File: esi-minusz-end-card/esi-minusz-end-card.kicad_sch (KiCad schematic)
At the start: 26 parts, among them J1 J-SAMTEC-TFM-120-01-L-D-RA, J2 U.FL-R-SMT-1, J3 M55-7101242R, J4 M55-7101242R, J5 M55-7101242R, J6 +UHF, J7 -UHF, J8 M55-7101242R, U1 NCS2-62+

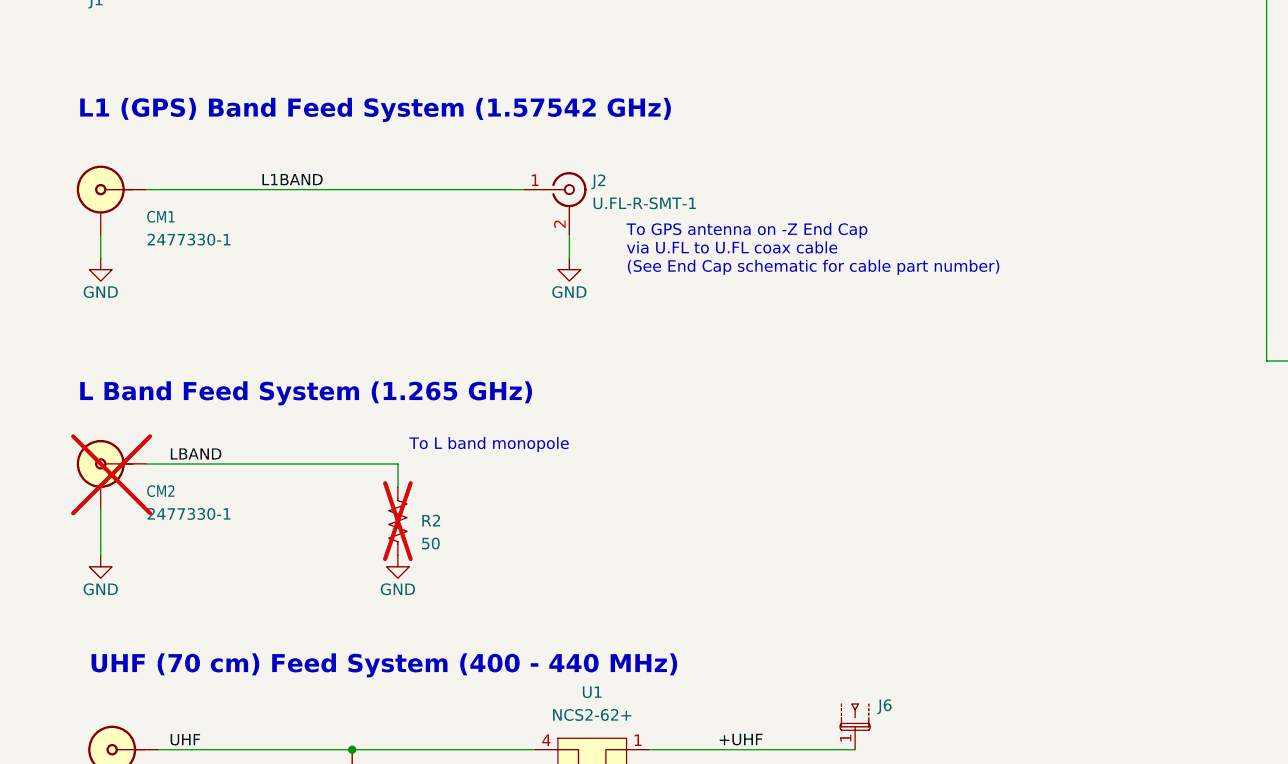
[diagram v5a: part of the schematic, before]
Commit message: Swapped L and L1 Bands
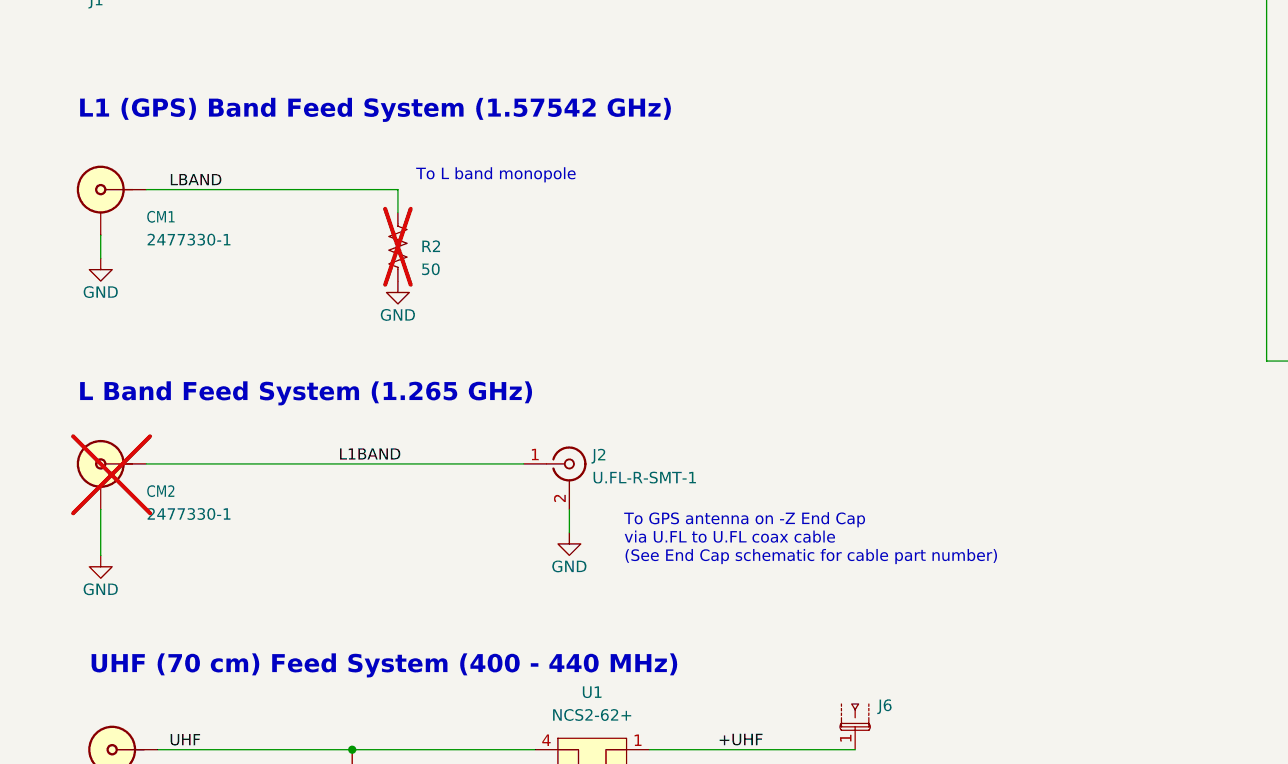
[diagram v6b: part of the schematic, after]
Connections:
- net L1BAND: now also CM2.SIG; no longer CM1.SIG
- net LBAND: now also CM1.SIG; no longer CM2.SIG
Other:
- moved on the sheet: J2, R2
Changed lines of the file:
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@@
 	(text "To L band monopole"
 		(exclude_from_sim no)
-		(at 102.87 184.15 0)
+		(at 103.632 154.178 0)
 		(effects
 			(font
@@
 	(text "To GPS antenna on -Z End Cap \nvia U.FL to U.FL coax cable\n(See End Cap schematic for cable part number)"
 		(exclude_from_sim no)
-		(at 127 164.465 0)
+		(at 126.746 196.596 0)
 		(effects
 			(font
@@
 	(wire
 		(pts
-			(xy 73.66 154.94) (xy 115.57 154.94)
+			(xy 73.66 185.42) (xy 115.57 185.42)
 		)
 		(stroke
@@
 	(wire
 		(pts
-			(xy 73.66 185.42) (xy 101.6 185.42)
+			(xy 73.66 154.94) (xy 101.6 154.94)
 		)
 		(stroke
@@
 	(wire
 		(pts
-			(xy 101.6 187.96) (xy 101.6 185.42)
+			(xy 101.6 157.48) (xy 101.6 154.94)
 		)
 		(stroke
@@
 	(wire
 		(pts
-			(xy 120.65 160.02) (xy 120.65 162.56)
+			(xy 120.65 190.5) (xy 120.65 193.04)
 		)
 		(stroke
@@
 	)
 	(label "L1BAND"
-		(at 86.36 154.94 0)
+		(at 94.996 185.42 0)
 		(effects
 			(font
@@
 	)
 	(label "LBAND"
-		(at 76.2 185.42 0)
+		(at 76.2 154.94 0)
 		(effects
 			(font
@@
 	(symbol
 		(lib_id "Connector:Conn_Coaxial")
-		(at 120.65 154.94 0)
+		(at 120.65 185.42 0)
 		(unit 1)
 		(body_style 1)
@@
 		(fields_autoplaced yes)
 		(property "Reference" "J2"
-			(at 123.19 153.9631 0)
+			(at 123.19 184.4431 0)
 			(show_name no)
 			(do_not_autoplace no)
@@
 		)
 		(property "Value" "U.FL-R-SMT-1"
-			(at 123.19 156.5031 0)
+			(at 123.19 186.9831 0)
 			(show_name no)
 			(do_not_autoplace no)
@@
 		)
 		(property "Footprint" "Connector_Coaxial:U.FL_Hirose_U.FL-R-SMT-1_Vertical"
-			(at 120.65 154.94 0)
+			(at 120.65 185.42 0)
 			(hide yes)
 			(show_name no)
@@
 		)
 		(property "Datasheet" "https://mm.digikey.com/Volume0/opasdata/d220001/medias/docus/4832/EDC3-302540-10.tif.pdf"
-			(at 120.65 154.94 0)
+			(at 120.65 185.42 0)
 			(hide yes)
 			(show_name no)
@@
 		)
 		(property "Description" "U.FL (UMCC) Connector Receptacle, Male Pin 50Ohm Surface Mount Solder"
-			(at 120.65 154.94 0)
+			(at 120.65 185.42 0)
 			(hide yes)
 			(show_name no)
@@
 		)
 		(property "DIS" "DigiKey"
-			(at 120.65 154.94 0)
+			(at 120.65 185.42 0)
 			(hide yes)
 			(show_name no)
@@
 		)
 		(property "DPN" "H11891CT-ND"
-			(at 120.65 154.94 0)
+			(at 120.65 185.42 0)
 			(hide yes)
 			(show_name no)
@@
 		)
 		(property "MFR" "Hirose"
-			(at 120.65 154.94 0)
+			(at 120.65 185.42 0)
 			(hide yes)
 			(show_name no)
@@
 		)
 		(property "MPN" "U.FL-R-SMT-1(10)"
-			(at 120.65 154.94 0)
+			(at 120.65 185.42 0)
 			(hide yes)
 			(show_name no)
@@
 	(symbol
 		(lib_id "power:GND")
-		(at 101.6 195.58 0)
+		(at 101.6 165.1 0)
 		(unit 1)
 		(body_style 1)
@@
 		(dnp no)
 		(property "Reference" "#PWR017"
-			(at 101.6 201.93 0)
+			(at 101.6 171.45 0)
 			(hide yes)
 			(show_name no)
@@
 		)
 		(property "Value" "GND"
-			(at 101.6 199.39 0)
+			(at 101.6 168.91 0)
 			(show_name no)
 			(do_not_autoplace no)
@@
 		)
 		(property "Footprint" ""
-			(at 101.6 195.58 0)
+			(at 101.6 165.1 0)
 			(hide yes)
 			(show_name no)
@@
 		)
 		(property "Datasheet" ""
-			(at 101.6 195.58 0)
+			(at 101.6 165.1 0)
 			(hide yes)
 			(show_name no)
@@
 		)
 		(property "Description" "Power symbol creates a global label with name \"GND\" , ground"
-			(at 101.6 195.58 0)
+			(at 101.6 165.1 0)
 			(hide yes)
 			(show_name no)
@@
 	(symbol
 		(lib_id "power:GND")
-		(at 120.65 162.56 0)
+		(at 120.65 193.04 0)
 		(unit 1)
 		(body_style 1)
@@
 		(dnp no)
 		(property "Reference" "#PWR11"
-			(at 120.65 168.91 0)
+			(at 120.65 199.39 0)
 			(hide yes)
 			(show_name no)
@@
 		)
 		(property "Value" "GND"
-			(at 120.65 166.37 0)
+			(at 120.65 196.85 0)
 			(show_name no)
 			(do_not_autoplace no)
@@
 		)
 		(property "Footprint" ""
-			(at 120.65 162.56 0)
+			(at 120.65 193.04 0)
 			(hide yes)
 			(show_name no)
@@
 		)
 		(property "Datasheet" ""
-			(at 120.65 162.56 0)
+			(at 120.65 193.04 0)
 			(hide yes)
 			(show_name no)
@@
 		)
 		(property "Description" "Power symbol creates a global label with name \"GND\" , ground"
-			(at 120.65 162.56 0)
+			(at 120.65 193.04 0)
 			(hide yes)
 			(show_name no)
@@
 	(symbol
 		(lib_id "Device:R_US")
-		(at 101.6 191.77 0)
+		(at 101.6 161.29 0)
 		(unit 1)
 		(body_style 1)
@@
 		(dnp yes)
 		(property "Reference" "R2"
-			(at 104.14 191.77 0)
+			(at 104.14 161.29 0)
 			(show_name no)
 			(do_not_autoplace no)
@@
 		)
 		(property "Value" "50"
-			(at 104.14 194.31 0)
+			(at 104.14 163.83 0)
 			(show_name no)
 			(do_not_autoplace no)
@@
 		)
 		(property "Footprint" "oresat-passives:0805-C-NOSILK"
-			(at 102.616 192.024 90)
+			(at 102.616 161.544 90)
 			(hide yes)
 			(show_name no)
@@
 		)
 		(property "Datasheet" ""
-			(at 101.6 191.77 0)
+			(at 101.6 161.29 0)
 			(hide yes)
 			(show_name no)
@@
 		)
 		(property "Description" "Resistor, US symbol"
-			(at 101.6 191.77 0)
+			(at 101.6 161.29 0)
 			(hide yes)
 			(show_name no)
